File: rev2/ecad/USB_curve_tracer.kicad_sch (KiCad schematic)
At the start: 26 parts, among them J1 DUT connector, J2 12V Bannana, J3 GND Bannana, U1 MCP4911, U3 MCP3204, U4 LM285Z-2.5

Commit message: restructuring and layout
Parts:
- removed J1: DUT connector, symbol Connector_Generic:Conn_01x02
- removed J2: 12V Bannana, symbol Connector:Conn_01x01_Socket
- removed J3: GND Bannana, symbol Connector:Conn_01x01_Socket
- added C2: 0.1uF, Capacitor_THT:C_Disc_D6.0mm_W2.5mm_P5.00mm, symbol Device:C
- added F1: 2A, Fuse:Fuse_1206_3216Metric_Pad1.42x1.75mm_HandSolder, symbol Device:Fuse
- added J1: DUT Connector, TerminalBlock_Phoenix:TerminalBlock_Phoenix_MKDS-1,5-2-5.08_1x02_P5.08mm_Horizontal, symbol Connector:Screw_Terminal_01x02
- added J2: Power Input, TerminalBlock_Phoenix:TerminalBlock_Phoenix_MKDS-1,5-2-5.08_1x02_P5.08mm_Horizontal, symbol Connector:Screw_Terminal_01x02
- D1: footprint (none) -> Diode_THT:D_DO-15_P10.16mm_Horizontal
- D6, D7: footprint LED_SMD:LED_1206_3216Metric_Pad1.42x1.75mm_HandSolder -> LED_THT:LED_D5.0mm
- U1: footprint (none) -> Package_DIP:DIP-8_W7.62mm
- U3: footprint (none) -> Package_DIP:DIP-14_W7.62mm
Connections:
- net +12V: now also F1.2
- net GND: now also C2.2, J2.1 (Pin_1)
- net IV_Variation/DUT+: now also J1.2 (Pin_2)
- net IV_Variation/DUT-: now also J1.1 (Pin_1)
- net at A1.9 (D6), R21.2, R22.1: now also C2.1
- net V/2: now reaches U3.3 (CH2)
- new net: F1.1, J2.2 (Pin_2)
- no-connect marks 21 -> 20
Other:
- company: Newton Technologies -> (none)
- moved on the sheet: A1, C3, D1, D6, D7, H1, H2, H3, H4, R11, R12, R21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

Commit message: layout
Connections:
- net V/2 renamed IV_Variation/V/4
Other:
- sheet IV_Variation ports: added V/4; removed none
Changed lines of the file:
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@@
     (rev "2")
     (comment 1 "Designed by Marek Newton")
+    (comment 2 "Unless otherwise noted, all resistor are 1% tolerance.")
   )
   (junction (at 62.23 182.88) (diameter 0) (color 0 0 0 0)
@@
     (stroke (width 0) (type default))
   )
-  (wire (pts (xy 140.97 68.58) (xy 146.05 68.58))
-    (stroke (width 0) (type default))
-  )
   (wire (pts (xy 148.59 33.02) (xy 148.59 34.29))
     (stroke (width 0) (type default))
@@
   )
   (wire (pts (xy 44.45 182.88) (xy 48.26 182.88))
+    (stroke (width 0) (type default))
+  )
+  (wire (pts (xy 120.65 68.58) (xy 146.05 68.58))
     (stroke (width 0) (type default))
   )
@@
   (text "Indication LEDs" (at 219.71 138.43 0)
     (effects (font (size 1.27 1.27)) (justify left bottom))
-  )
-  (global_label "V{slash}2" (shape input) (at 140.97 68.58 180) (fields_autoplaced)
-    (effects (font (size 1.27 1.27)) (justify right))
-    (property "Intersheetrefs" "${INTERSHEET_REFS}" (at 134.4356 68.58 0)
-      (effects (font (size 1.27 1.27)) (justify right) hide)
-    )
   )
   (symbol (lib_id "Device:R_US") (at 139.7 38.1 0) (unit 1)
@@
       (effects (font (size 1.27 1.27)) (justify left))
     )
-    (instances
+    (pin "V{slash}4" output (at 120.65 68.58 0)
+      (effects (font (size 1.27 1.27)) (justify right))
+    )
+    (instances

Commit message: BOM
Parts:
- removed U4: LM285Z-2.5, Package_TO_SOT_THT:TO-92_Inline, symbol Reference_Voltage:LM285Z-2.5
- added U4: LM385BZ-2.5, Package_TO_SOT_THT:TO-92_Inline, symbol Reference_Voltage:LM385BZ-2.5
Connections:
- net GND: now also U4.3 (A)
- net at R24.2, R25.2, R26.2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: now also U4.2 (K)
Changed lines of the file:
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@@
+    )
+  )
+  (symbol (lib_id "Reference_Voltage:LM385BZ-2.5") (at 129.54 48.26 90) (unit 1)
+    (in_bom yes) (on_board yes) (dnp no) (fields_autoplaced)
+    (property "Reference" "U4" (at 132.08 47.625 90)
+      (effects (font (size 1.27 1.27)) (justify right))
+    )
+    (property "Value" "LM385BZ-2.5" (at 132.08 50.165 90)
+      (effects (font (size 1.27 1.27)) (justify right))
+    )
+    (property "Footprint" "Package_TO_SOT_THT:TO-92_Inline" (at 134.62 48.26 0)
+      (effects (font (size 1.27 1.27) italic) hide)
+    )
+    (property "Datasheet" "http://www.onsemi.com/pub_link/Collateral/LM285-D.PDF" (at 129.54 48.26 0)
+      (effects (font (size 1.27 1.27) italic) hide)
+    )
+    (pin "2")
+    (pin "3")
+    (instances
+      (project "USB_curve_tracer"
+        (path "/e63e39d7-6ac0-4ffd-8aa3-1841a4541b55"
+          (reference "U4") (unit 1)
+        )
+      )
     )
   )
@@
         )
       )
-    )
-  )
-  (symbol (lib_id "Reference_Voltage:LM285Z-2.5") (at 129.54 48.26 90) (unit 1)
-    (in_bom yes) (on_board yes) (dnp no) (fields_autoplaced)
-    (property "Reference" "U4" (at 132.08 47.625 90)
-      (effects (font (size 1.27 1.27)) (justify right))
-    )
-    (property "Value" "LM285Z-2.5" (at 132.08 50.165 90)
-      (effects (font (size 1.27 1.27)) (justify right))
-    )
-    (property "Footprint" "Package_TO_SOT_THT:TO-92_Inline" (at 134.62 48.26 0)
-      (effects (font (size 1.27 1.27) italic) hide)
-    )
-    (property "Datasheet" "http://www.onsemi.com/pub_link/Collateral/LM285-D.PDF" (at 129.54 48.26 0)
-      (effects (font (size 1.27 1.27) italic) hide)
-    )
-    (pin "2")
-    (pin "3")
-    (instances
-      (project "USB_curve_tracer"
-        (path "/e63e39d7-6ac0-4ffd-8aa3-1841a4541b55"
-          (reference "U4") (unit 1)
-        )
-      )

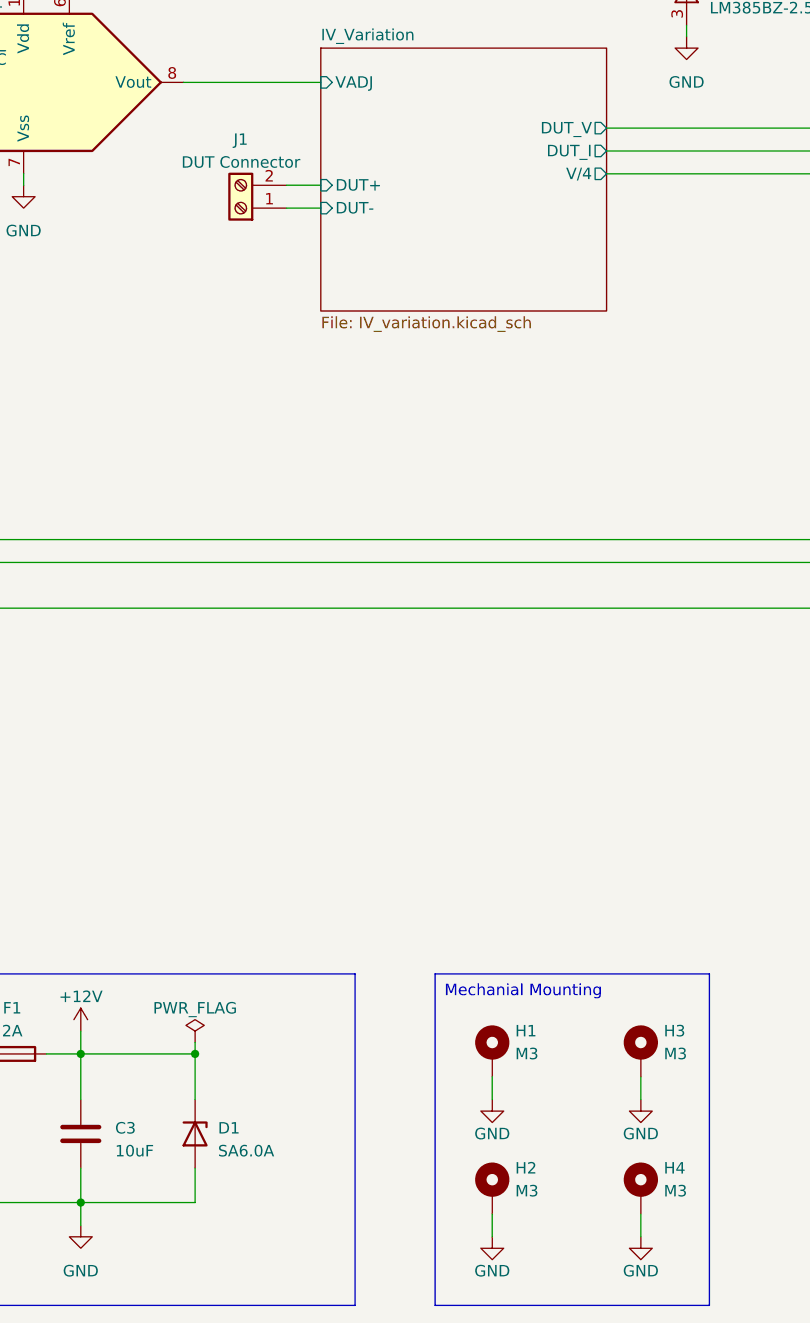
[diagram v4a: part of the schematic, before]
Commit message: Linear Output
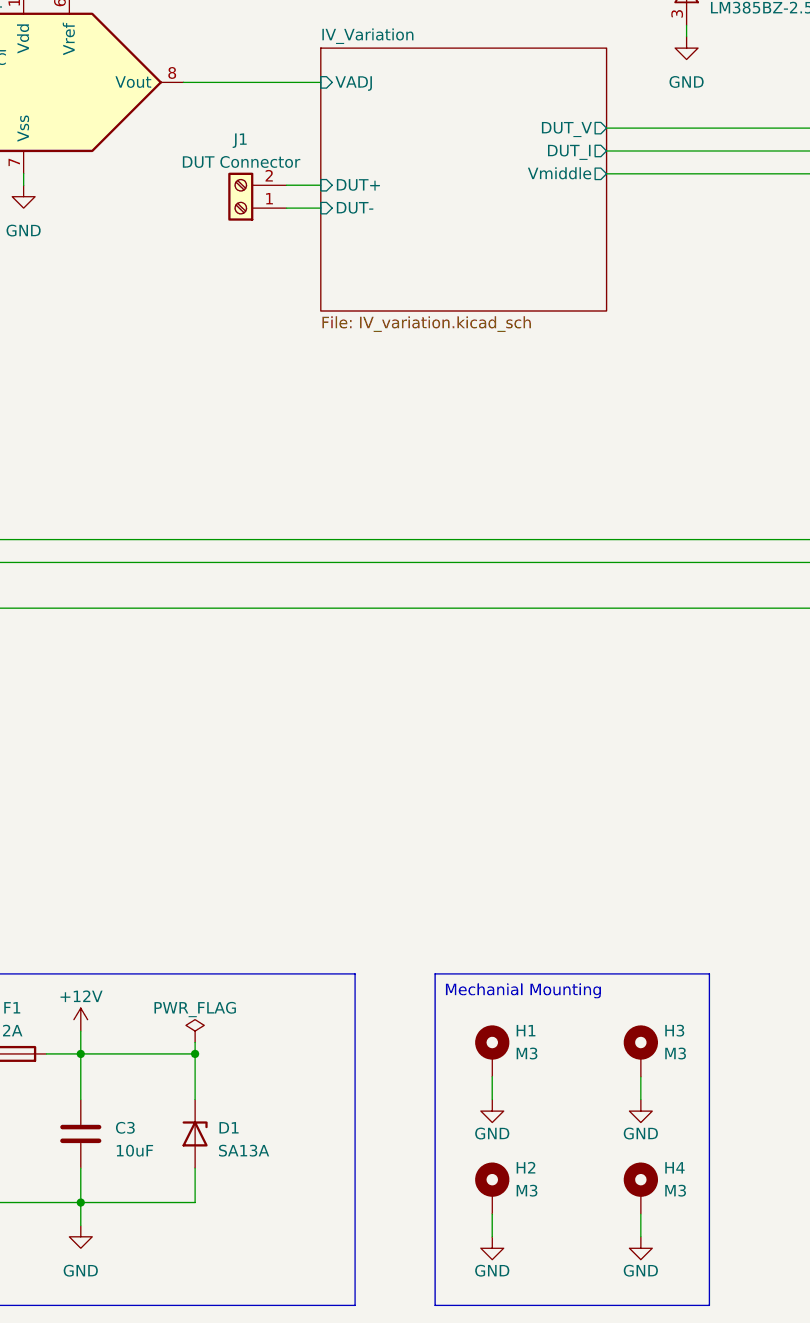
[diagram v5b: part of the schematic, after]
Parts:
- D1: value SA6.0A -> SA13A
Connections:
- net IV_Variation/V/4 renamed IV_Variation/Vmiddle
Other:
- sheet IV_Variation ports: added Vmiddle; removed V/4
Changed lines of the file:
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@@
       (effects (font (size 1.27 1.27)) (justify left))
     )
-    (property "Value" "SA6.0A" (at 77.47 177.165 90)
+    (property "Value" "SA13A" (at 77.47 177.165 90)
       (effects (font (size 1.27 1.27)) (justify left))
     )
@@
       (effects (font (size 1.27 1.27)) (justify left))
     )
-    (pin "V{slash}4" output (at 120.65 68.58 0)
+    (pin "Vmiddle" output (at 120.65 68.58 0)
       (effects (font (size 1.27 1.27)) (justify right))
     )
